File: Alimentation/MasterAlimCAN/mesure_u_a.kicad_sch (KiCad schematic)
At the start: 5 parts, among them U7 ACS711xEXLT-15AB

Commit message: Init placement for MasterAlimCAN
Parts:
- renumbered C19 to C18, R17 to R16, R18 to R17, R19 to R18, U7 to U6

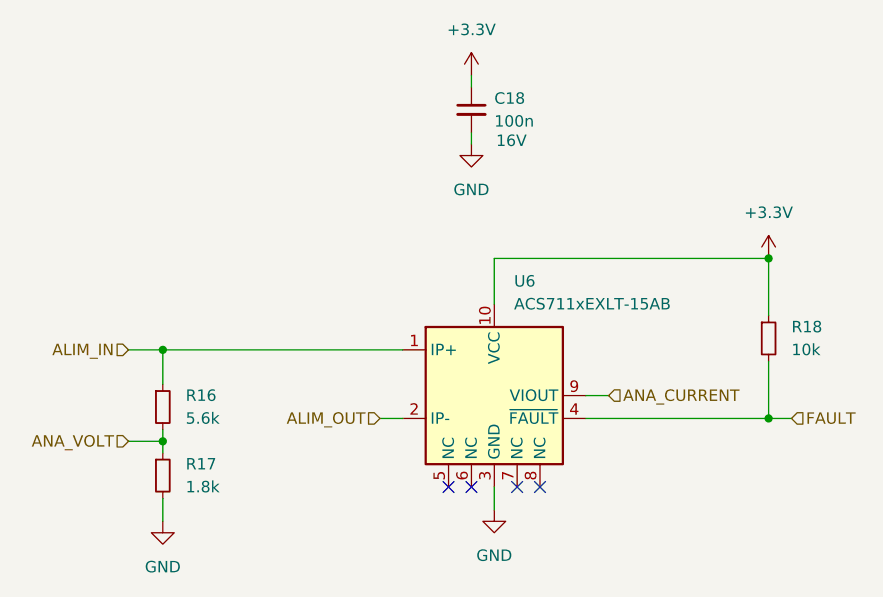
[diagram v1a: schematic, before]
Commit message: New disposition for alim CAN
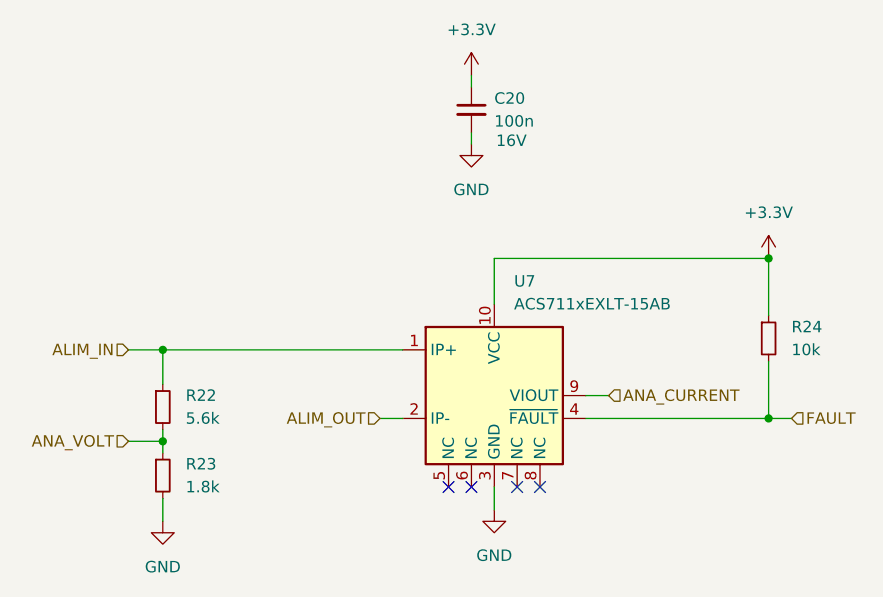
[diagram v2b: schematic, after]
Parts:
- renumbered C18 to C20, R16 to R22, R17 to R23, R18 to R24, U6 to U7
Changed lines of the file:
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@@
   (symbol (lib_id "power:+3.3V") (at 166.37 68.58 0) (unit 1)
     (in_bom yes) (on_board yes) (dnp no) (fields_autoplaced)
-    (property "Reference" "#PWR070" (at 166.37 72.39 0)
+    (property "Reference" "#PWR075" (at 166.37 72.39 0)
       (effects (font (size 1.27 1.27)) hide)
     )
@@
     (instances
       (project "MasterAlimCAN"
-        (path "/c83bc042-587c-48f9-abdb-41233c8ec938/d13bc51e-4a46-4c07-a6c6-d21a8a578dbb"
-          (reference "#PWR070") (unit 1)
-        )
         (path "/c83bc042-587c-48f9-abdb-41233c8ec938/286e504b-a3e5-45a7-aff1-29d1bab3e070"
           (reference "#PWR075") (unit 1)
@@
   (symbol (lib_id "power:+3.3V") (at 133.35 48.26 0) (unit 1)
     (in_bom yes) (on_board yes) (dnp no) (fields_autoplaced)
-    (property "Reference" "#PWR067" (at 133.35 52.07 0)
+    (property "Reference" "#PWR072" (at 133.35 52.07 0)
       (effects (font (size 1.27 1.27)) hide)
     )
@@
     (instances
       (project "MasterAlimCAN"
-        (path "/c83bc042-587c-48f9-abdb-41233c8ec938/d13bc51e-4a46-4c07-a6c6-d21a8a578dbb"
-          (reference "#PWR067") (unit 1)
-        )
         (path "/c83bc042-587c-48f9-abdb-41233c8ec938/286e504b-a3e5-45a7-aff1-29d1bab3e070"
           (reference "#PWR072") (unit 1)
@@
   (symbol (lib_id "power:GND") (at 99.06 97.79 0) (unit 1)
     (in_bom yes) (on_board yes) (dnp no) (fields_autoplaced)
-    (property "Reference" "#PWR066" (at 99.06 104.14 0)
+    (property "Reference" "#PWR071" (at 99.06 104.14 0)
       (effects (font (size 1.27 1.27)) hide)
     )
@@
     (instances
       (project "MasterAlimCAN"
-        (path "/c83bc042-587c-48f9-abdb-41233c8ec938/d13bc51e-4a46-4c07-a6c6-d21a8a578dbb"
-          (reference "#PWR066") (unit 1)
-        )
         (path "/c83bc042-587c-48f9-abdb-41233c8ec938/286e504b-a3e5-45a7-aff1-29d1bab3e070"
           (reference "#PWR071") (unit 1)
@@
   (symbol (lib_id "power:GND") (at 133.35 55.88 0) (unit 1)
     (in_bom yes) (on_board yes) (dnp no) (fields_autoplaced)
-    (property "Reference" "#PWR068" (at 133.35 62.23 0)
+    (property "Reference" "#PWR073" (at 133.35 62.23 0)
       (effects (font (size 1.27 1.27)) hide)
     )
@@
     (instances
       (project "MasterAlimCAN"
-        (path "/c83bc042-587c-48f9-abdb-41233c8ec938/d13bc51e-4a46-4c07-a6c6-d21a8a578dbb"
-          (reference "#PWR068") (unit 1)
-        )
         (path "/c83bc042-587c-48f9-abdb-41233c8ec938/286e504b-a3e5-45a7-aff1-29d1bab3e070"
           (reference "#PWR073") (unit 1)
@@
   (symbol (lib_id "Device:R_Small") (at 99.06 85.09 0) (unit 1)
     (in_bom yes) (on_board yes) (dnp no) (fields_autoplaced)
-    (property "Reference" "R16" (at 101.6 83.82 0)
+    (property "Reference" "R22" (at 101.6 83.82 0)
       (effects (font (size 1.27 1.27)) (justify left))
     )
@@
     (instances
       (project "MasterAlimCAN"
-        (path "/c83bc042-587c-48f9-abdb-41233c8ec938/d13bc51e-4a46-4c07-a6c6-d21a8a578dbb"
-          (reference "R16") (unit 1)
-        )
         (path "/c83bc042-587c-48f9-abdb-41233c8ec938/d9896301-8add-4d80-8eb5-da1ffd619a30"
           (reference "R22") (unit 1)
@@
   (symbol (lib_id "power:GND") (at 135.89 96.52 0) (unit 1)
     (in_bom yes) (on_board yes) (dnp no) (fields_autoplaced)
-    (property "Reference" "#PWR069" (at 135.89 102.87 0)
+    (property "Reference" "#PWR074" (at 135.89 102.87 0)
       (effects (font (size 1.27 1.27)) hide)
     )
@@
     (instances
       (project "MasterAlimCAN"
-        (path "/c83bc042-587c-48f9-abdb-41233c8ec938/d13bc51e-4a46-4c07-a6c6-d21a8a578dbb"
-          (reference "#PWR069") (unit 1)
-        )
         (path "/c83bc042-587c-48f9-abdb-41233c8ec938/286e504b-a3e5-45a7-aff1-29d1bab3e070"
           (reference "#PWR074") (unit 1)
@@
   (symbol (lib_id "Device:C_Small") (at 133.35 52.07 0) (unit 1)
     (in_bom yes) (on_board yes) (dnp no)
-    (property "Reference" "C18" (at 135.89 50.8063 0)
+    (property "Reference" "C20" (at 135.89 50.8063 0)
       (effects (font (size 1.27 1.27)) (justify left))
     )
@@
     (instances
       (project "MasterAlimCAN"
-        (path "/c83bc042-587c-48f9-abdb-41233c8ec938/d13bc51e-4a46-4c07-a6c6-d21a8a578dbb"
-          (reference "C18") (unit 1)
-        )
         (path "/c83bc042-587c-48f9-abdb-41233c8ec938/d9896301-8add-4d80-8eb5-da1ffd619a30"
           (reference "C20") (unit 1)
@@
   (symbol (lib_id "Sensor_Current:ACS711xEXLT-15AB") (at 135.89 83.82 0) (unit 1)
     (in_bom yes) (on_board yes) (dnp no) (fields_autoplaced)
-    (property "Reference" "U6" (at 138.0841 71.12 0)
+    (property "Reference" "U7" (at 138.0841 71.12 0)
       (effects (font (size 1.27 1.27)) (justify left))
     )
@@
     (instances
       (project "MasterAlimCAN"
-        (path "/c83bc042-587c-48f9-abdb-41233c8ec938/d13bc51e-4a46-4c07-a6c6-d21a8a578dbb"
-          (reference "U6") (unit 1)
-        )
         (path "/c83bc042-587c-48f9-abdb-41233c8ec938/286e504b-a3e5-45a7-aff1-29d1bab3e070"
           (reference "U7") (unit 1)
@@
   (symbol (lib_id "Device:R_Small") (at 166.37 77.47 0) (unit 1)
     (in_bom yes) (on_board yes) (dnp no) (fields_autoplaced)
-    (property "Reference" "R18" (at 168.91 76.2 0)
+    (property "Reference" "R24" (at 168.91 76.2 0)
       (effects (font (size 1.27 1.27)) (justify left))
     )
@@
     (instances
       (project "MasterAlimCAN"
-        (path "/c83bc042-587c-48f9-abdb-41233c8ec938/d13bc51e-4a46-4c07-a6c6-d21a8a578dbb"
-          (reference "R18") (unit 1)
-        )
         (path "/c83bc042-587c-48f9-abdb-41233c8ec938/d9896301-8add-4d80-8eb5-da1ffd619a30"
           (reference "R24") (unit 1)
@@
   (symbol (lib_id "Device:R_Small") (at 99.06 92.71 0) (unit 1)
     (in_bom yes) (on_board yes) (dnp no) (fields_autoplaced)
-    (property "Reference" "R17" (at 101.6 91.44 0)
+    (property "Reference" "R23" (at 101.6 91.44 0)
       (effects (font (size 1.27 1.27)) (justify left))
     )
@@
     (instances
       (project "MasterAlimCAN"
-        (path "/c83bc042-587c-48f9-abdb-41233c8ec938/d13bc51e-4a46-4c07-a6c6-d21a8a578dbb"
-          (reference "R17") (unit 1)
-        )
         (path "/c83bc042-587c-48f9-abdb-41233c8ec938/d9896301-8add-4d80-8eb5-da1ffd619a30"
           (reference "R23") (unit 1)
